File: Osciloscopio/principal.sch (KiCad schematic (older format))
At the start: 0 parts

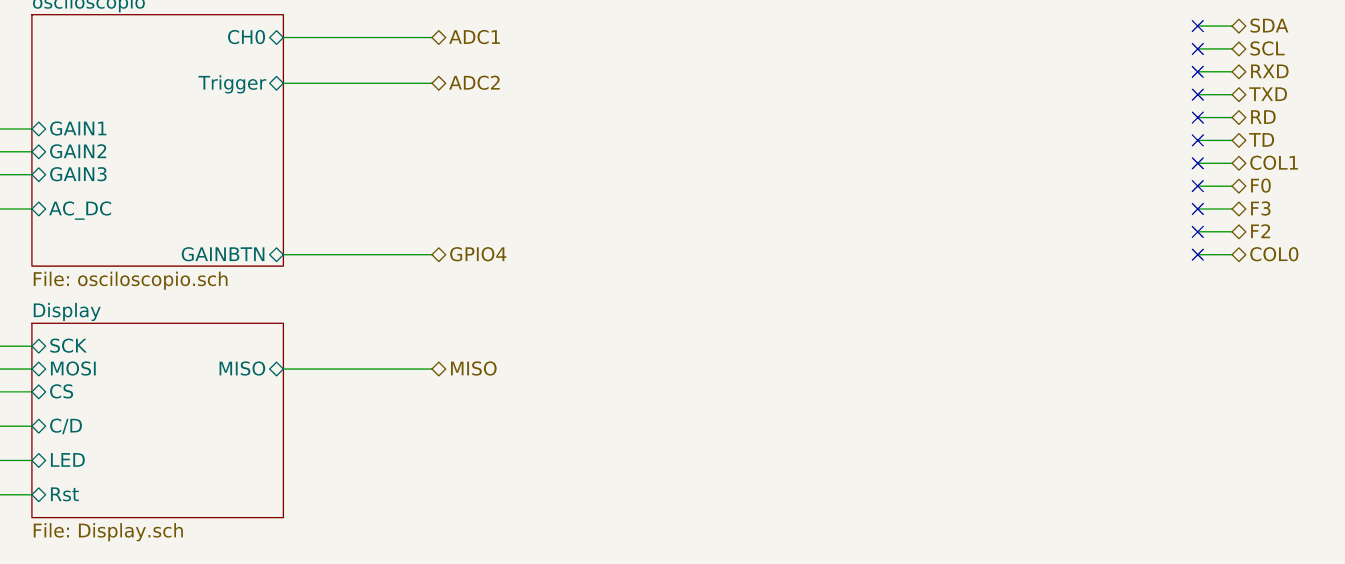
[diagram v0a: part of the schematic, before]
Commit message: Se definen los footprints y numeros de parte de todos los componentes Se elimina el Boton de Gain dado que un solo boton es insuficiente para controlar el osciloscopio y no se disponen de señales digitales suficientes para controlar varios botones. Se decide por ende colocar el display cerca de los botones de la EDU-CIAA de modo que se pueda colocar en el display la función de los botones.
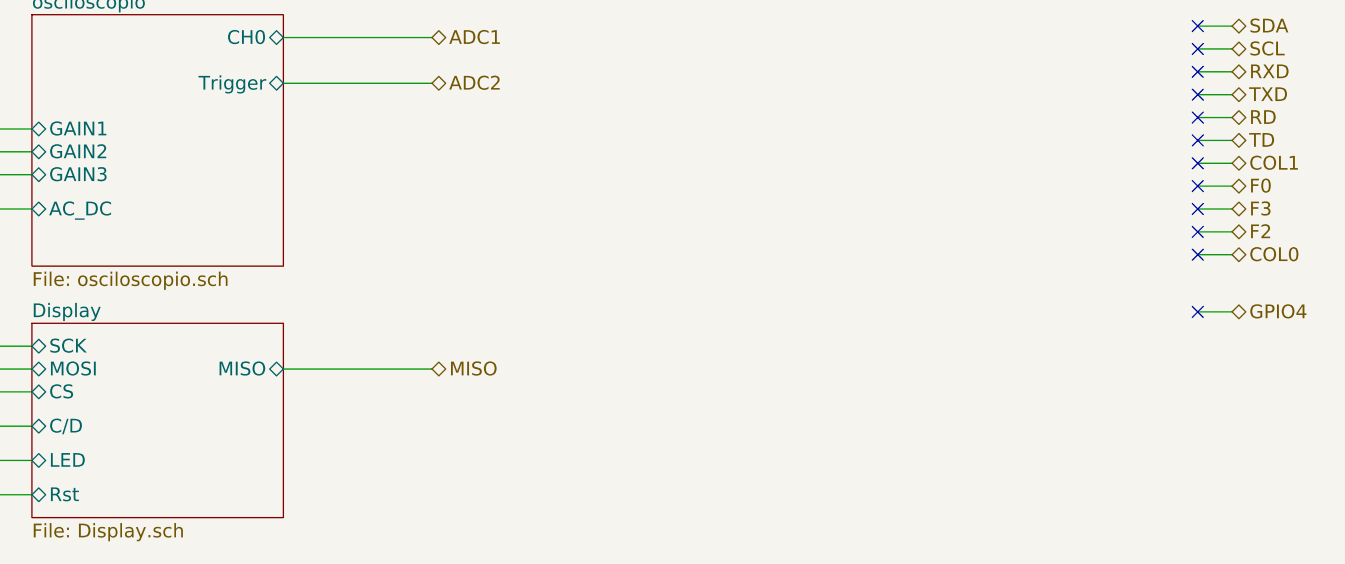
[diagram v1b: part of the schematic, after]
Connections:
- no-connect marks 33 -> 34
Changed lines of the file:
@@
 F5 "GAIN3" B L 5050 2800 60
 F6 "CH0" B R 6150 2200 60
-F7 "GAINBTN" B R 6150 3150 60
-F8 "Trigger" B R 6150 2400 60
+F7 "Trigger" B R 6150 2400 60
 $EndSheet
-Text HLabel 6800 3150 2    60   BiDi ~ 0
-GPIO4
-Wire Wire Line
-	6150 3150 6800 3150
 $Sheet
 S 5050 3450 1100 850
@@
 Wire Wire Line
 	10300 1350 10150 1350
+Text HLabel 10300 3400 2    60   BiDi ~ 0
+GPIO4
+NoConn ~ 10150 3400
+Wire Wire Line
+	10150 3400 10300 3400
 $EndSCHEMATC

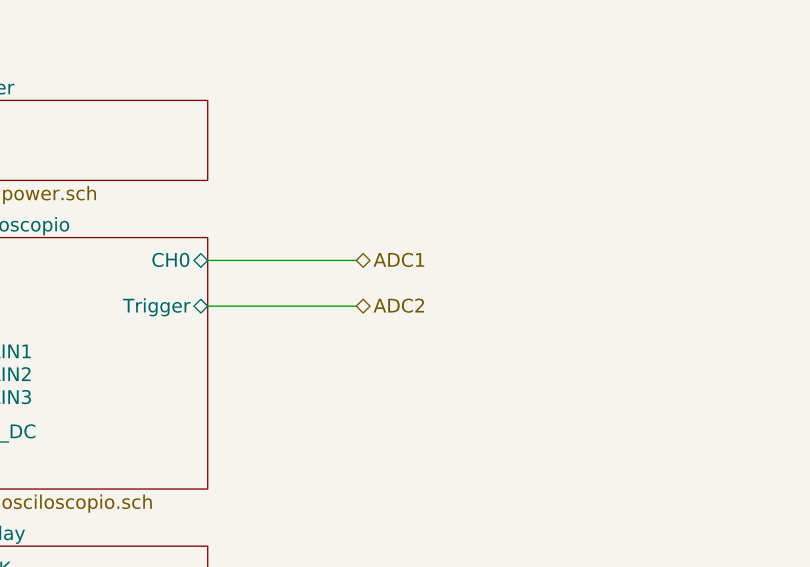
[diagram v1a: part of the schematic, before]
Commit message: Se realiza el Placement de los componentes y un prerouteo para mostrar que el placement elegido permite un adecuado routeo del mismo.
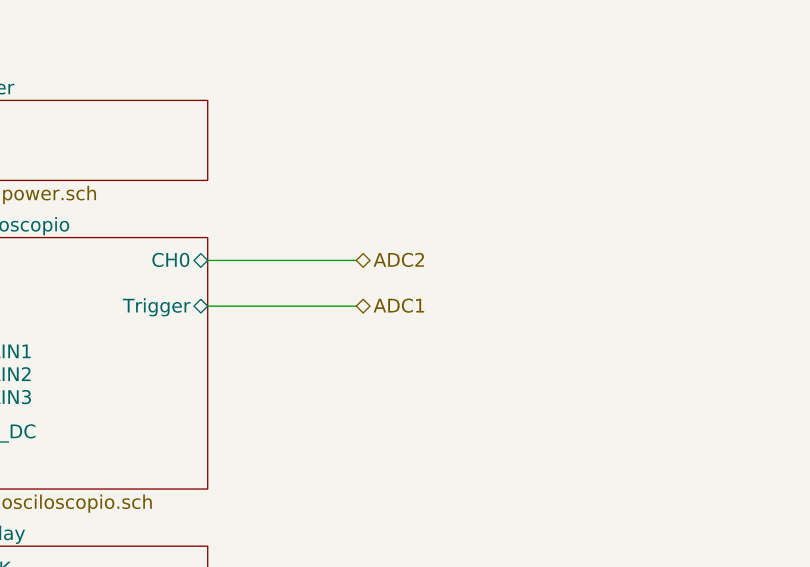
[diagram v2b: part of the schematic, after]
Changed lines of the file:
@@
 Text HLabel 10300 1650 2    60   BiDi ~ 0
 ADC3
-Text HLabel 6800 2400 2    60   BiDi ~ 0
+Text HLabel 6800 2200 2    60   BiDi ~ 0
 ADC2
 NoConn ~ 1450 1000
@@
 Wire Wire Line
 	4400 2950 5050 2950
-Text HLabel 6800 2200 2    60   BiDi ~ 0
+Text HLabel 6800 2400 2    60   BiDi ~ 0
 ADC1
 Wire Wire Line

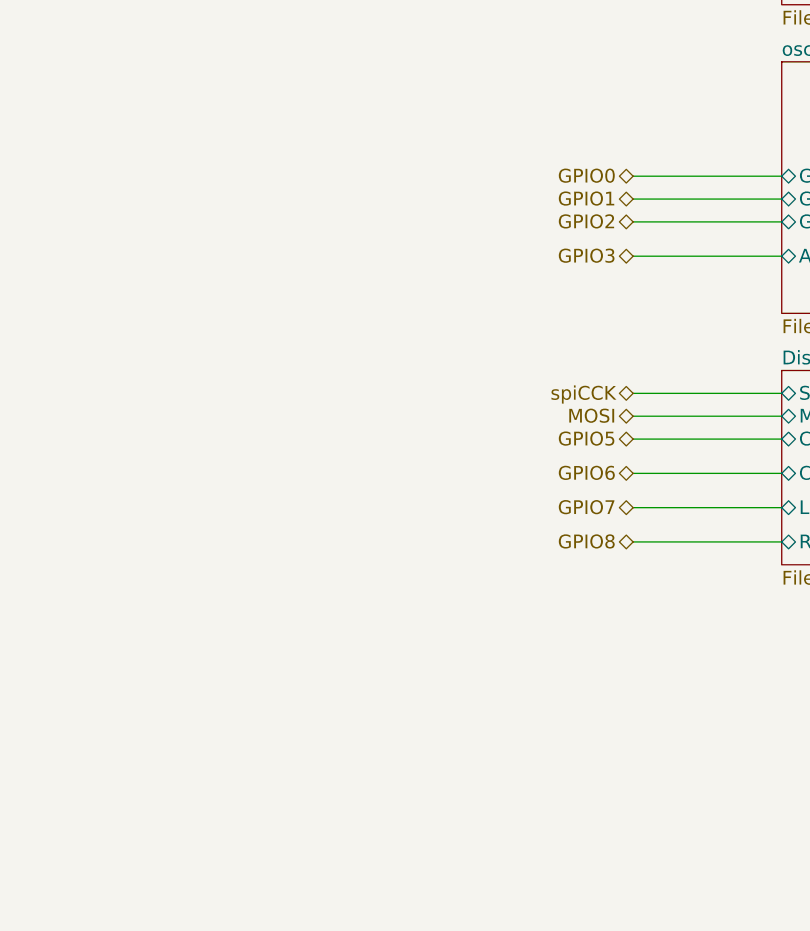
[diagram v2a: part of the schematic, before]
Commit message: Se finaliza el prerouteo y se realizan las primeras correcciones de la revision
Este routeo cumple chequeo de DRC pero no es definitivo, le faltan planos y detalles finos.

Se realiza este commit antes de continuar con los demas cambios sugeridos por la revisión que son más peligrosos, como quitar una hoja del esquematico y quitar todos aquellos pines del AX1 que no se están utilizando
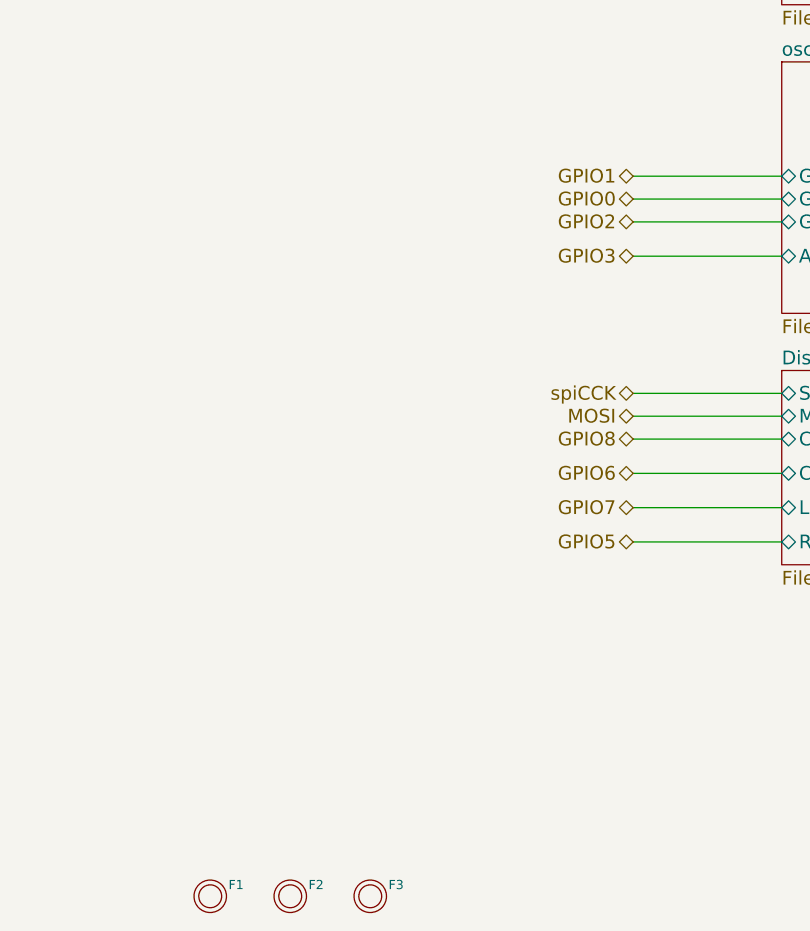
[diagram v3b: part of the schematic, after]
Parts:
- added F1, F2, F3: FIDUCIAL, osc:Fiducial_1mm, symbol FIDUCIAL
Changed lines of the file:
@@
 LIBS:power
 LIBS:conn
+LIBS:ej2cese
 LIBS:Oscilloscopio-cache
 EELAYER 25 0
@@
 Comment1 "https://github.com/ciaa/Ponchos/tree/master/modelos/doc"
 Comment2 "Autores y Licencia del template (Diego Brengi - UNLaM)"
-Comment3 "Autor del poncho Nicolás Dassieu Blanchet. Ver directorio \"doc\""
+Comment3 "Autor Nicolás Dassieu Blanchet - Curso Diseño de PCB del CESE - Ver directorio \"doc\" "
 Comment4 "CÓDIGO PONCHO:"
 $EndDescr
@@
 Text HLabel 1300 1500 0    60   BiDi ~ 0
 COL2
-Text HLabel 4400 4200 0    60   BiDi ~ 0
+Text HLabel 4400 3750 0    60   BiDi ~ 0
 GPIO8
 Text HLabel 4400 4050 0    60   BiDi ~ 0
@@
 Text HLabel 4400 3900 0    60   BiDi ~ 0
 GPIO6
-Text HLabel 4400 3750 0    60   BiDi ~ 0
+Text HLabel 4400 4200 0    60   BiDi ~ 0
 GPIO5
 Text HLabel 1350 3500 0    60   BiDi ~ 0
@@
 F1 "power.sch" 60
 $EndSheet
+Text HLabel 4400 2600 0    60   BiDi ~ 0
+GPIO1
 Text HLabel 4400 2700 0    60   BiDi ~ 0
-GPIO1
-Text HLabel 4400 2600 0    60   BiDi ~ 0
 GPIO0
 Text HLabel 4400 2950 0    60   BiDi ~ 0
@@
 Wire Wire Line
 	10150 3400 10300 3400
+$Comp
+L FIDUCIAL F1
+U 1 1 5797EA60
+P 2550 5750
+F 0 "F1" H 2630 5800 40  0000 L CNN
+F 1 "FIDUCIAL" H 2550 5650 30  0001 C CNN
+F 2 "osc:Fiducial_1mm" H 2550 5800 60  0001 C CNN
+F 3 "" H 2550 5800 60  0001 C CNN
+F 4 "FIDUCIAL" H 2600 5550 60  0001 C CNN "Descripcion"
+	1    2550 5750
+	1    0    0    -1
+$EndComp
+$Comp
+L FIDUCIAL F2
+U 1 1 5797EC0A
+P 2900 5750
+F 0 "F2" H 2980 5800 40  0000 L CNN
+F 1 "FIDUCIAL" H 2900 5650 30  0001 C CNN
+F 2 "osc:Fiducial_1mm" H 2900 5800 60  0001 C CNN
+F 3 "" H 2900 5800 60  0001 C CNN
+F 4 "FIDUCIAL" H 2950 5550 60  0001 C CNN "Descripcion"
+	1    2900 5750
+	1    0    0    -1
+$EndComp
+$Comp
+L FIDUCIAL F3
+U 1 1 5797FEC6
+P 3250 5750
+F 0 "F3" H 3330 5800 40  0000 L CNN
+F 1 "FIDUCIAL" H 3250 5650 30  0001 C CNN
+F 2 "osc:Fiducial_1mm" H 3250 5800 60  0001 C CNN
+F 3 "" H 3250 5800 60  0001 C CNN
+F 4 "FIDUCIAL" H 3300 5550 60  0001 C CNN "Descripcion"
+	1    3250 5750
+	1    0    0    -1
+$EndComp
 $EndSCHEMATC

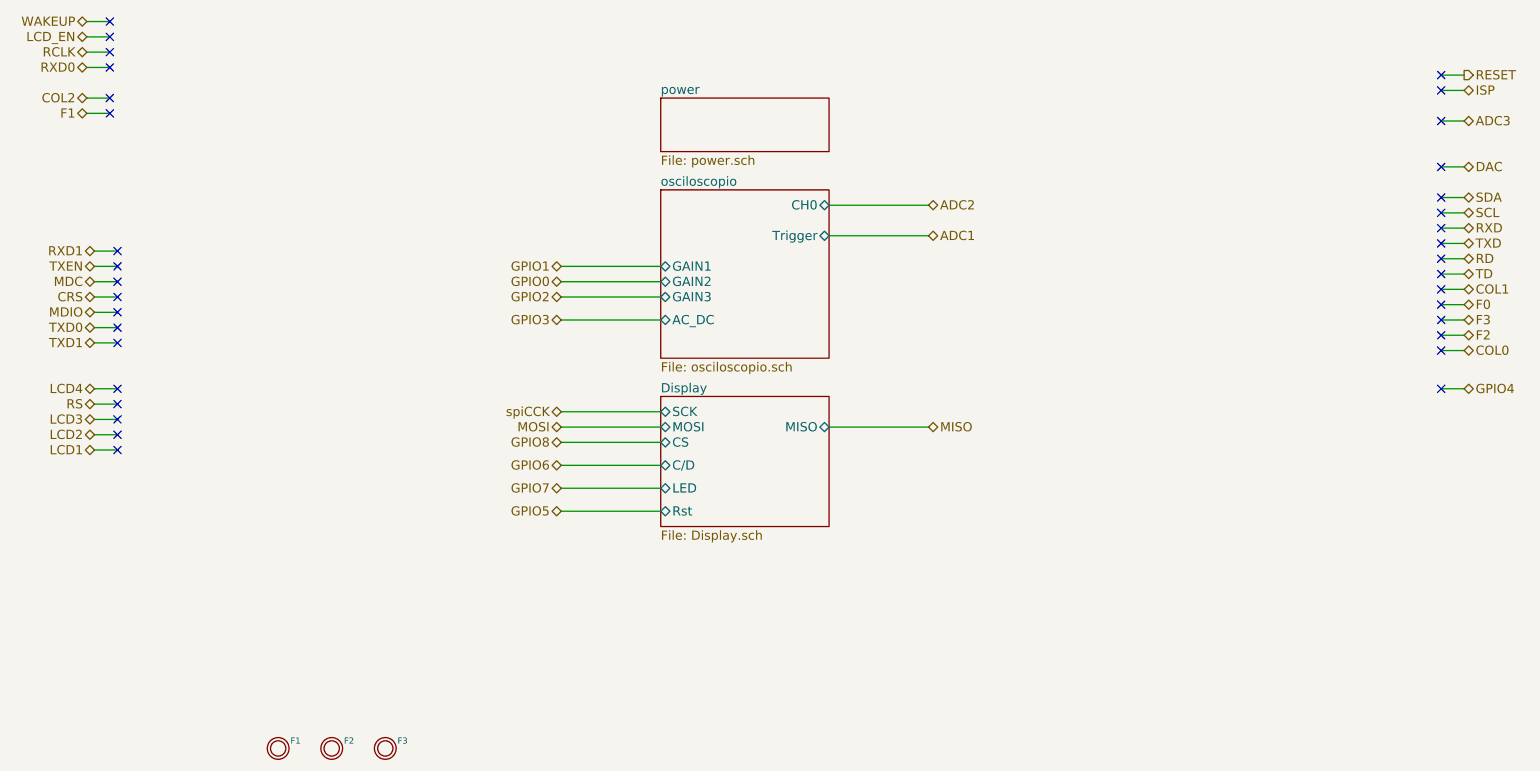
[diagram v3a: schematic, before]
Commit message: Se finalizan las correciones sugeridas a nivel esquematico
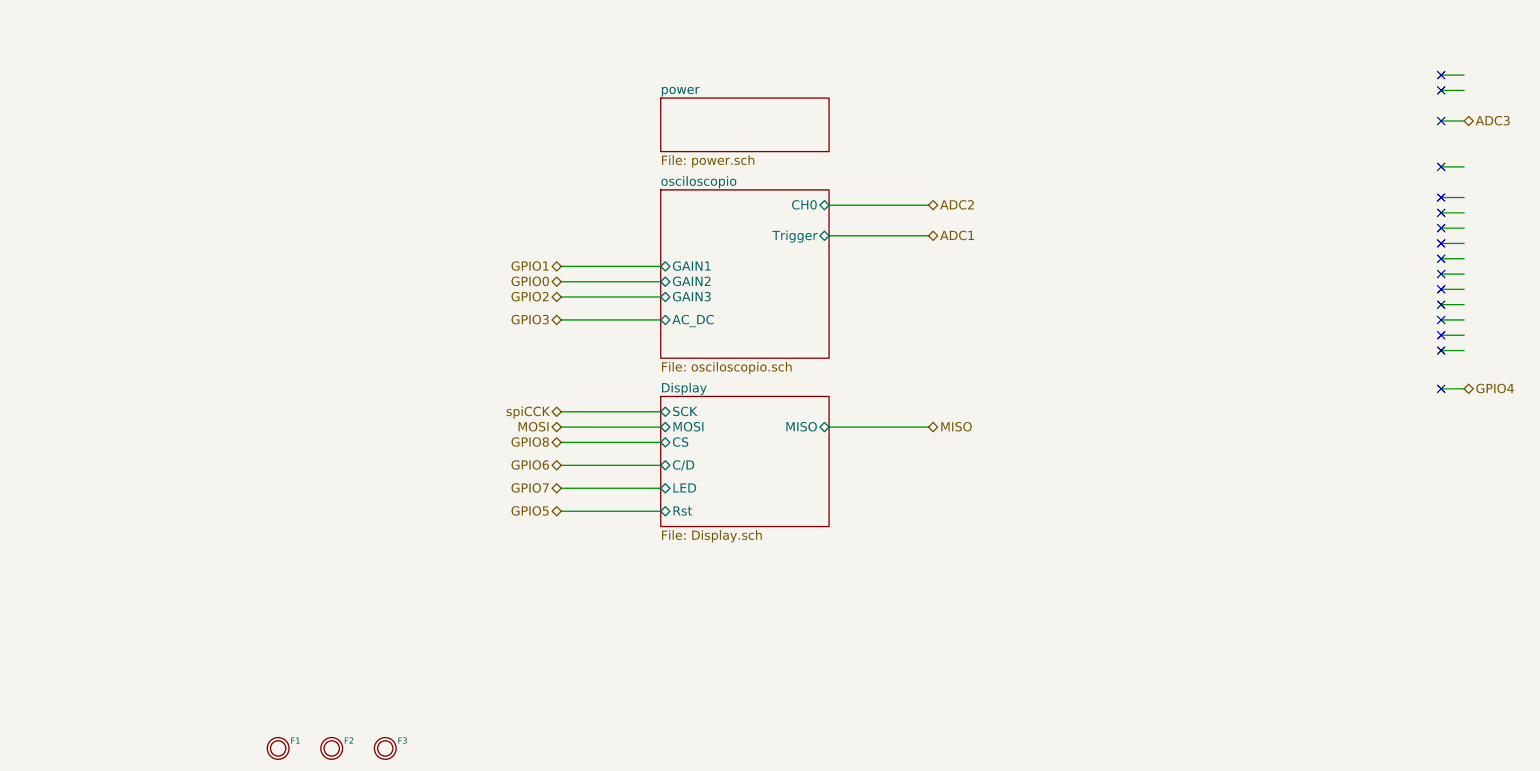
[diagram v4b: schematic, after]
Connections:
- net labels removed: COL0, COL1, COL2, CRS, DAC, F0, F1, F2, F3, ISP, LCD1, LCD2, LCD3, LCD4, LCD_EN, MDC, MDIO, RCLK, RD, RESET, RS, RXD, RXD0, RXD1, SCL, SDA, TD, TXD, TXD0, TXD1, TXEN, WAKEUP
- wire segments 47 -> 29
- no-connect marks 34 -> 16
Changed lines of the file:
@@
 EESchema Schematic File Version 2
-LIBS:Poncho_Esqueleto
-LIBS:Misc_Poncho_Grande
-LIBS:device
-LIBS:texas
 LIBS:osc
-LIBS:power
-LIBS:conn
-LIBS:ej2cese
 LIBS:Oscilloscopio-cache
 EELAYER 25 0
@@
 Comment4 "CÓDIGO PONCHO:"
 $EndDescr
-Text HLabel 1300 1000 0    60   BiDi ~ 0
-WAKEUP
-Text HLabel 1300 1500 0    60   BiDi ~ 0
-COL2
 Text HLabel 4400 3750 0    60   BiDi ~ 0
 GPIO8
@@
 Text HLabel 4400 4200 0    60   BiDi ~ 0
 GPIO5
-Text HLabel 1350 3500 0    60   BiDi ~ 0
-RS
-Text HLabel 1300 1100 0    60   BiDi ~ 0
-LCD_EN
-Text HLabel 1350 3400 0    60   BiDi ~ 0
-LCD4
-Text HLabel 1350 3600 0    60   BiDi ~ 0
-LCD3
-Text HLabel 1350 3700 0    60   BiDi ~ 0
-LCD2
-Text HLabel 1350 3800 0    60   BiDi ~ 0
-LCD1
 Text HLabel 6800 3650 2    60   BiDi ~ 0
 MISO
@@
 Text HLabel 4400 3550 0    60   BiDi ~ 0
 spiCCK
-Text HLabel 1350 2900 0    60   BiDi ~ 0
-MDIO
-Text HLabel 1350 2800 0    60   BiDi ~ 0
-CRS
-Text HLabel 1350 2700 0    60   BiDi ~ 0
-MDC
-Text HLabel 1350 2500 0    60   BiDi ~ 0
-RXD1
-Text HLabel 1300 1300 0    60   BiDi ~ 0
-RXD0
-Text HLabel 1350 2600 0    60   BiDi ~ 0
-TXEN
-Text HLabel 1350 3100 0    60   BiDi ~ 0
-TXD1
-Text HLabel 1350 3000 0    60   BiDi ~ 0
-TXD0
-Text HLabel 1300 1200 0    60   BiDi ~ 0
-RCLK
-Text HLabel 10300 2950 2    60   BiDi ~ 0
-F3
-Text HLabel 10300 3050 2    60   BiDi ~ 0
-F2
-Text HLabel 1300 1600 0    60   BiDi ~ 0
-F1
-Text HLabel 10300 2850 2    60   BiDi ~ 0
-F0
-Text HLabel 10300 2750 2    60   BiDi ~ 0
-COL1
-Text HLabel 10300 3150 2    60   BiDi ~ 0
-COL0
-Text HLabel 10300 2650 2    60   BiDi ~ 0
-TD
-Text HLabel 10300 2550 2    60   BiDi ~ 0
-RD
-Text HLabel 10300 2450 2    60   BiDi ~ 0
-TXD
-Text HLabel 10300 2350 2    60   BiDi ~ 0
-RXD
-Text HLabel 10300 2250 2    60   BiDi ~ 0
-SCL
-Text HLabel 10300 2150 2    60   BiDi ~ 0
-SDA
-Text HLabel 10300 1450 2    60   BiDi ~ 0
-ISP
-Text HLabel 10300 1350 2    60   Output ~ 0
-RESET
-Text HLabel 10300 1950 2    60   BiDi ~ 0
-DAC
 Text HLabel 10300 1650 2    60   BiDi ~ 0
 ADC3
 Text HLabel 6800 2200 2    60   BiDi ~ 0
 ADC2
-NoConn ~ 1450 1000
-NoConn ~ 1450 1100
-NoConn ~ 1450 1200
-NoConn ~ 1450 1300
-NoConn ~ 1450 1500
-NoConn ~ 1450 1600
-Wire Wire Line
-	1450 1000 1300 1000
-Wire Wire Line
-	1300 1100 1450 1100
-Wire Wire Line
-	1300 1200 1450 1200
-Wire Wire Line
-	1300 1300 1450 1300
-Wire Wire Line
-	1300 1500 1450 1500
-Wire Wire Line
-	1300 1600 1450 1600
 $Sheet
 S 5050 1500 1100 350
@@
 Wire Wire Line
 	6150 3650 6800 3650
-NoConn ~ 1500 2900
-NoConn ~ 1500 3000
-NoConn ~ 1500 3100
-Wire Wire Line
-	1350 2900 1500 2900
-Wire Wire Line
-	1350 3000 1500 3000
-Wire Wire Line
-	1350 3100 1500 3100
-NoConn ~ 1500 2600
-NoConn ~ 1500 2700
-NoConn ~ 1500 2800
-Wire Wire Line
-	1350 2600 1500 2600
-Wire Wire Line
-	1350 2700 1500 2700
-Wire Wire Line
-	1350 2800 1500 2800
-NoConn ~ 1500 2500
-Wire Wire Line
-	1350 2500 1500 2500
-NoConn ~ 1500 3600
-NoConn ~ 1500 3700
-NoConn ~ 1500 3800
-Wire Wire Line
-	1350 3600 1500 3600
-Wire Wire Line
-	1350 3700 1500 3700
-Wire Wire Line
-	1350 3800 1500 3800
-NoConn ~ 1500 3400
-NoConn ~ 1500 3500
-Wire Wire Line
-	1350 3400 1500 3400
-Wire Wire Line
-	1350 3500 1500 3500
 NoConn ~ 10150 2450
 NoConn ~ 10150 2350
